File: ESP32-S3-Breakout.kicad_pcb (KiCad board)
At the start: 4 copper layers, 29 x 54.4 mm, 34 parts, among them J1 USB_C_Receptacle_USB2.0, J2 USB_C_Receptacle_USB2.0, J3 Conn_01x21, J4 Conn_01x21, Q1 Q_NPN_BCE, Q2 Q_NPN_BCE, SW1 SW_Push, SW2 SW_Push, U1 USBLC6-2SC6, U2 USBLC6-2SC6, U3 ESP32-S3-WROOM, U4 CH340C, U5 XC6210B332MR, Y1 32.768kHz

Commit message: initial group of modifications.
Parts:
- removed FB2: 500mA?, Inductor_SMD:L_0603_1608Metric
- removed J4: Conn_01x21, Connector_PinHeader_2.54mm:PinHeader_1x21_P2.54mm_Vertical
- removed U4: CH340C, Package_SO:SOIC-16_3.9x9.9mm_P1.27mm
- added C10: 4.7uF, Capacitor_SMD:C_0603_1608Metric, F.Cu at (94.3, 126.6)
- added C11: 1uF, Capacitor_SMD:C_0603_1608Metric, F.Cu at (79.7, 126.5)
- added C12: 10uF, Capacitor_SMD:C_0603_1608Metric, F.Cu at (92.4, 103.3)
- added C13: 10uF, Capacitor_SMD:C_0603_1608Metric, F.Cu at (93.9, 122.2)
- added C14: 10uF, Capacitor_SMD:C_0603_1608Metric, F.Cu at (85.1, 112.1)
- added C15: 100nF, Capacitor_SMD:C_0603_1608Metric, F.Cu at (78.6, 122.1)
- added C16: 100nF, Capacitor_SMD:C_0603_1608Metric, F.Cu at (80.2, 122.1)
- added C17: 100nF, Capacitor_SMD:C_0603_1608Metric, F.Cu at (81.8, 122.1)
- added C18: 15pF, Capacitor_SMD:C_0603_1608Metric, F.Cu at (86.7, 112.1)
- added C19: 15pF, Capacitor_SMD:C_0603_1608Metric, F.Cu at (94.3, 112.1)
- added D3: LED, LED_SMD:LED_0603_1608Metric, F.Cu at (76.8, 130.8)
- added Q3: FDC6330L, Package_TO_SOT_SMD:TSOT-23-6, F.Cu at (91.2, 108.6)
- added R10: 100k, Resistor_SMD:R_0603_1608Metric, F.Cu at (86.7, 108.7)
- added R11: 100, Resistor_SMD:R_0603_1608Metric, F.Cu at (85.1, 108.7)
- added R8: 1k, Resistor_SMD:R_0603_1608Metric, F.Cu at (92.7, 112.1)
- added R9: 100k, Resistor_SMD:R_0603_1608Metric, F.Cu at (88.3, 108.7)
- added U6: USBLC6-2SC6, Package_TO_SOT_SMD:SOT-23-6, F.Cu at (89.7, 121.7)
- added Y2: 12Mhz, Crystal:Crystal_SMD_SeikoEpson_TSX3225-4Pin_3.2x2.5mm, F.Cu at (89.7, 112.1)
- C1: value 22u -> 22uF; footprint Capacitor_SMD:C_0805_2012Metric -> Capacitor_SMD:C_0603_1608Metric
- C2, C4: value 18p -> 15pF
- C3: value 0.1u -> 100nF
- C5: value 1u -> 100nF
- C6, C7: value 0.1u -> 1uF
- C8, C9: value 1u -> 1uF; footprint Capacitor_SMD:C_0805_2012Metric -> Capacitor_SMD:C_0603_1608Metric
- D2: value 1N5819WS -> WS2812B-2020; footprint Diode_SMD:D_SOD-323 -> LED_SMD:LED_WS2812B-2020_PLCC4_2.0x2.0mm
- FB1: value 500mA? -> 500mA; footprint Inductor_SMD:L_0603_1608Metric -> Fuse:Fuse_0603_1608Metric
- J1: value USB_C_Receptacle_USB2.0 -> USB_TYPE_C_16PIN; footprint Connector_USB:USB_C_Receptacle_HRO_TYPE-C-31-M-12 -> Connector_USB:USB_C_Receptacle_GCT_USB4105-xx-A_16P_TopMnt_Horizontal
- J2: value USB_C_Receptacle_USB2.0 -> Conn_01x22; footprint Connector_USB:USB_C_Receptacle_HRO_TYPE-C-31-M-12 -> Connector_PinHeader_2.54mm:PinHeader_1x22_P2.54mm_Vertical; moved to B.Cu
- J3: value Conn_01x21 -> Conn_01x22; footprint Connector_PinHeader_2.54mm:PinHeader_1x21_P2.54mm_Vertical -> Connector_PinHeader_2.54mm:PinHeader_1x22_P2.54mm_Vertical
- Q1, Q2: value Q_NPN_BCE -> S8050
- R3: value 5.1k -> 1k
- R4: value 5.1k -> 10k
- SW1: value SW_Push -> RESET
- SW2: value SW_Push -> BOOT
- U1: value USBLC6-2SC6 -> CH343P; footprint Package_TO_SOT_SMD:SOT-23-6 -> Package_DFN_QFN:QFN-16-1EP_3x3mm_P0.5mm_EP1.7x1.7mm
- U2: value USBLC6-2SC6 -> CH334F; footprint Package_TO_SOT_SMD:SOT-23-6 -> Package_DFN_QFN:QFN-24-1EP_4x4mm_P0.5mm_EP2.7x2.7mm
- U3: value ESP32-S3-WROOM -> ESP32-S3-WROOM-1-N16R8
- moved J2 51.1 mm to (75.6, 74.2), turned to 180 degrees
- moved R5 23.4 mm to (94.3, 125.0), turned to 180 degrees
- moved J3 22.3 mm to (98.4, 74.2)
- moved C8 19.6 mm to (95.5, 122.2), turned to -90 degrees
- moved C3 18.7 mm to (80.0, 100.0), turned to 180 degrees
- moved C1 15.9 mm to (83.2, 100.0), turned to 0 degrees
- moved FB1 15.9 mm to (83.5, 122.1), turned to -90 degrees
- moved SW2 15.8 mm to (79.7, 129.9)
- moved C4 14.6 mm to (93.4, 100.0), turned to 0 degrees
- moved D2 14.5 mm to (81.9, 103.3), turned to 0 degrees
- moved SW1 14.4 mm to (94.3, 129.9)
- moved R1 14.3 mm to (87.1, 122.1), turned to 90 degrees
- moved C7 13.9 mm to (94.3, 117.8), turned to 180 degrees
- moved C2 13.7 mm to (86.4, 100.0), turned to 0 degrees
- moved Y1 13.6 mm to (89.9, 100.2), turned to 0 degrees
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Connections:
- net /CC1_1 renamed /ESP32-S3/CC1_1
- net /CC2_1 renamed /ESP32-S3/CC2_1
- C1 pad 1: +3V3 -> +3.3V
- C2 pad 2: /IO15 -> /GPIO15
- C3 pad 1: +3V3 -> +3.3V
- C4 pad 1: /IO16 -> /GPIO16
- C5 pad 1: /EN -> +3.3V
- C6 pad 1: +3V3 -> /ESP32-S3/3.3VUSB
- C7 pad 1: +3V3 -> GND
- C7 pad 2: GND -> /ESP32-S3/3.3VUSB
- C9 pad 1: +3V3 -> +3.3V
- D1 pad 2: /VBUS1 -> /ESP32-S3/VBUS
- D2 pad 1: Net-(D2-Pad1) -> /LED_OUT
- D2 pad 2: /VBUS2 -> GND
- J1 pad A4: /VBUS1 -> /ESP32-S3/VBUS
- J1 pad A6: /USB_UART_D+ -> /ESP32-S3/USB_D+
- J1 pad A7: /USB_UART_D- -> /ESP32-S3/USB_D-
- J1 pad A9: /VBUS1 -> /ESP32-S3/VBUS
- J1 pad B4: /VBUS1 -> /ESP32-S3/VBUS
- J1 pad B6: /USB_UART_D+ -> /ESP32-S3/USB_D+
- J1 pad B7: /USB_UART_D- -> /ESP32-S3/USB_D-
- J1 pad B9: /VBUS1 -> /ESP32-S3/VBUS
- J3 pad 10: /IO17 -> /GPIO38
- J3 pad 11: /IO18 -> /GPIO37
- J3 pad 12: /IO8 -> /GPIO36
- J3 pad 13: /IO19 -> /GPIO35
- J3 pad 14: /IO20 -> /GPIO0
- J3 pad 15: /IO3 -> /GPIO45
- J3 pad 16: /IO46 -> /GPIO48
- J3 pad 17: /IO9 -> /GPIO47
- J3 pad 18: /IO10 -> /GPIO21
- J3 pad 19: /IO11 -> /ESP_USB+
- J3 pad 2: +3V3 -> /ESP_TX0
- J3 pad 20: /IO12 -> /ESP_USB-
- J3 pad 21: +5V -> GND
- J3 pad 3: /EN -> /ESP_RX0
- J3 pad 4: /IO4 -> /GPIO1
- J3 pad 5: /IO5 -> /GPIO2
- J3 pad 6: /IO6 -> /GPIO42
- J3 pad 7: /IO7 -> /GPIO41
- J3 pad 8: /IO15 -> /GPIO40
- J3 pad 9: /IO16 -> /GPIO39
- Q1 pad 2: /EN -> /ENABLE
- Q1 pad 3: /RTS -> /ESP32-S3/RTS
- Q2 pad 2: /IO0 -> /GPIO0
- Q2 pad 3: /DTR -> /ESP32-S3/DTR
- R3 pad 1: /CC1_2 -> +3.3V
- R3 pad 2: GND -> Net-(D3-A)
- R4 pad 1: /CC2_2 -> /GPIO0
- R4 pad 2: GND -> +3.3V
- R5 pad 1: +3V3 -> +3.3V
- R5 pad 2: /EN -> /ENABLE
- R6 pad 1: /DTR -> /ESP32-S3/DTR
- R7 pad 1: /RTS -> /ESP32-S3/RTS
- SW1 pad 1: /IO0 -> /ENABLE
- SW2 pad 1: /EN -> /GPIO0
- U1 pad 1: /IO19 -> /ESP32-S3/3.3VUSB
- U1 pad 3: /IO20 -> /ESP32-S3/3.3VUSB
- U1 pad 4: /USB_D+ -> /ESP_RX0
- U1 pad 5: /VBUS2 -> /ESP_TX0
- U1 pad 6: /USB_D- -> /ESP32-S3/3.3VUSB
- U2 pad 1: /UART_D- -> unconnected-(U2-~{OVCUR}-Pad1)
- U2 pad 2: GND -> unconnected-(U2-Pad2)
- U2 pad 3: /UART_D+ -> Net-(U2-XOUT)
- U2 pad 4: /USB_UART_D+ -> Net-(U2-XIN)
- U2 pad 5: /VBUS1 -> unconnected-(U2-D-4-Pad5)
- U2 pad 6: /USB_UART_D- -> unconnected-(U2-D+4-Pad6)
- U3 pad 10: /IO17 -> /GPIO17
- U3 pad 11: /IO18 -> /GPIO18
- U3 pad 12: /IO8 -> /GPIO8
- U3 pad 13: /IO19 -> /ESP_USB-
- U3 pad 14: /IO20 -> /ESP_USB+
- U3 pad 15: /IO3 -> /GPIO3
- U3 pad 16: /IO46 -> /GPIO46
- U3 pad 17: /IO9 -> /GPIO9
- U3 pad 18: /IO10 -> /GPIO10
- U3 pad 19: /IO11 -> /GPIO11
- U3 pad 2: +3V3 -> +3.3V
- U3 pad 20: /IO12 -> /GPIO12
- U3 pad 21: /IO13 -> /GPIO13
- U3 pad 22: /IO14 -> /GPIO14
- U3 pad 23: /IO21 -> /GPIO21
- U3 pad 24: /IO47 -> /GPIO47
- U3 pad 25: /IO48 -> /GPIO48
- U3 pad 26: /IO45 -> /GPIO45
- U3 pad 27: /IO0 -> /GPIO0
- U3 pad 28: /IO35 -> /GPIO35
- U3 pad 29: /IO36 -> /GPIO36
- U3 pad 3: /EN -> /ENABLE
- U3 pad 30: /IO37 -> /GPIO37
- U3 pad 31: /IO38 -> /GPIO38
- U3 pad 32: /IO39 -> /GPIO39
- U3 pad 33: /IO40 -> /GPIO40
- U3 pad 34: /IO41 -> /GPIO41
- U3 pad 35: /IO42 -> /GPIO42
- U3 pad 36: /RXD0 -> /ESP_RX0
- U3 pad 37: /TXD0 -> /ESP_TX0
- U3 pad 38: /IO2 -> /GPIO2
- U3 pad 39: /IO1 -> /GPIO1
- U3 pad 4: /IO4 -> /GPIO4
- U3 pad 5: /IO5 -> /GPIO5
- U3 pad 6: /IO6 -> /GPIO6
- U3 pad 7: /IO7 -> /GPIO7
- U3 pad 8: /IO15 -> /GPIO15
- U3 pad 9: /IO16 -> /GPIO16
- U5 pad 5: +3V3 -> +3.3V
- Y1 pad 1: /IO16 -> /GPIO16
- Y1 pad 2: /IO15 -> /GPIO15
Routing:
- net /EN: track 52.0 -> 0.00 mm, vias 4 -> 0
- net GND: track 42.0 -> 0.00 mm, vias 13 -> 0
- net /IO12: track 33.2 -> 0.00 mm, vias 1 -> 0
- net /IO0: track 31.6 -> 0.00 mm, vias 3 -> 0
- net /TXD0: track 31.1 -> 0.00 mm, vias 2 -> 0
- net /RXD0: track 30.5 -> 0.00 mm, vias 2 -> 0
- net /IO13: track 29.3 -> 0.00 mm, vias 1 -> 0
- net /IO19: track 27.6 -> 0.00 mm, vias 1 -> 0
- net /IO11: track 27.4 -> 0.00 mm, vias 1 -> 0
- net /IO14: track 26.7 -> 0.00 mm, vias 1 -> 0
- net /IO10: track 24.5 -> 0.00 mm, vias 1 -> 0
- net /IO21: track 23.8 -> 0.00 mm, vias 1 -> 0
- net /IO20: track 22.6 -> 0.00 mm, vias 1 -> 0
- net /IO9: track 22.2 -> 0.00 mm, vias 1 -> 0
- net /IO47: track 19.7 -> 0.00 mm, vias 1 -> 0
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- added copper zone on B.Cu, net GND
- added copper zone on F.Cu, net GND
- added copper zone on In2.Cu, net GND
- removed copper zone on F.Cu, net +3V3
- removed copper zone on In2.Cu, net +3V3
- removed copper zone on B.Cu, net +5V
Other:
- board size 29 x 54.4 mm -> 25.4 x 63.3 mm
- board text removed: "3V3"
- board text removed: "5V"
- board text removed: "EN"
- board text removed: "ESP32-S3 DEV Module"
- board text removed: "GND"
- board text removed: "IO0"
- board text removed: "IO1"
- board text removed: "IO10"
- board text removed: "IO11"
- board text removed: "IO12"
- board text removed: "IO13"
- board text removed: "IO14"
- board text removed: "IO15"
- board text removed: "IO16"
- board text removed: "IO17"
- board text removed: "IO18"
- board text removed: "IO19"
- board text removed: "IO2"
- board text removed: "IO20"
- board text removed: "IO21"
- board text removed: "IO3"
- board text removed: "IO35"
- board text removed: "IO36"
- board text removed: "IO37"
- board text removed: "IO38"
- board text removed: "IO39"
- board text removed: "IO4"
- board text removed: "IO40"
- board text removed: "IO41"
- board text removed: "IO42"
- board text removed: "IO45"
- board text removed: "IO46"
- board text removed: "IO47"
- board text removed: "IO48"
- board text removed: "IO5"
- board text removed: "IO6"
- board text removed: "IO7"
- board text removed: "IO8"
- board text removed: "IO9"
- board text removed: "RXD0"
- board text removed: "Rev 1 12/2022"
- board text removed: "TXD0"
- board text removed: "UART"
- board text removed: "USB"

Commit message: board is fully routed.
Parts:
- U1: footprint Package_DFN_QFN:QFN-16-1EP_3x3mm_P0.5mm_EP1.7x1.7mm -> Package_DFN_QFN:QFN-16-1EP_3x3mm_P0.5mm_EP1.7x1.7mm_ThermalVias
- U2: footprint Package_DFN_QFN:QFN-24-1EP_4x4mm_P0.5mm_EP2.7x2.7mm -> Package_DFN_QFN:QFN-24-1EP_4x4mm_P0.5mm_EP2.7x2.7mm_ThermalVias
- moved Q1 0.95 mm to (79.1, 108.8)
- moved Q2 0.95 mm to (79.1, 112.4)
- moved R6 0.95 mm to (81.9, 112.4)
- moved R7 0.95 mm to (81.9, 108.8)
- turned D2 to 90 degrees
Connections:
- U2 pad 10: /ESP32-S3/UART_D+ -> /ESP_USB+
- U2 pad 11: /ESP_USB- -> /ESP32-S3/UART_D-
- U2 pad 12: /ESP_USB+ -> /ESP32-S3/UART_D+
- U2 pad 9: /ESP32-S3/UART_D- -> /ESP_USB-
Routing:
- net +3.3V: track 0.00 -> 112.6 mm, vias 0 -> 2
- net /ENABLE: track 0.00 -> 94.8 mm, vias 0 -> 2
- net /GPIO0: track 0.00 -> 68.5 mm, vias 0 -> 3
- net /ESP_TX0: track 0.00 -> 60.5 mm, vias 0 -> 2
- net /ESP_RX0: track 0.00 -> 54.3 mm, vias 0 -> 3
- net +5V: track 0.00 -> 53.3 mm, vias 0 -> 3
- net /ESP_USB-: track 0.00 -> 51.1 mm, vias 0 -> 3
- net /ESP32-S3/3.3VUSB: track 0.00 -> 47.4 mm, vias 0 -> 2
- net /ESP_USB+: track 0.00 -> 47.4 mm, vias 0 -> 3
- net /GPIO38: track 0.00 -> 36.4 mm, vias 0 -> 2
- net /ESP32-S3/VBUS: track 0.00 -> 35.6 mm, vias 0 -> 5
- net /GPIO15: track 0.00 -> 34.8 mm, vias 0 -> 2
- net /GPIO16: track 0.00 -> 33.6 mm, vias 0 -> 3
- net /GPIO14: track 0.00 -> 33.2 mm, vias 0 -> 1
- net /GPIO13: track 0.00 -> 30.4 mm, vias 0 -> 1
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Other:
- board size 25.4 x 63.3 mm -> 25.4 x 60 mm

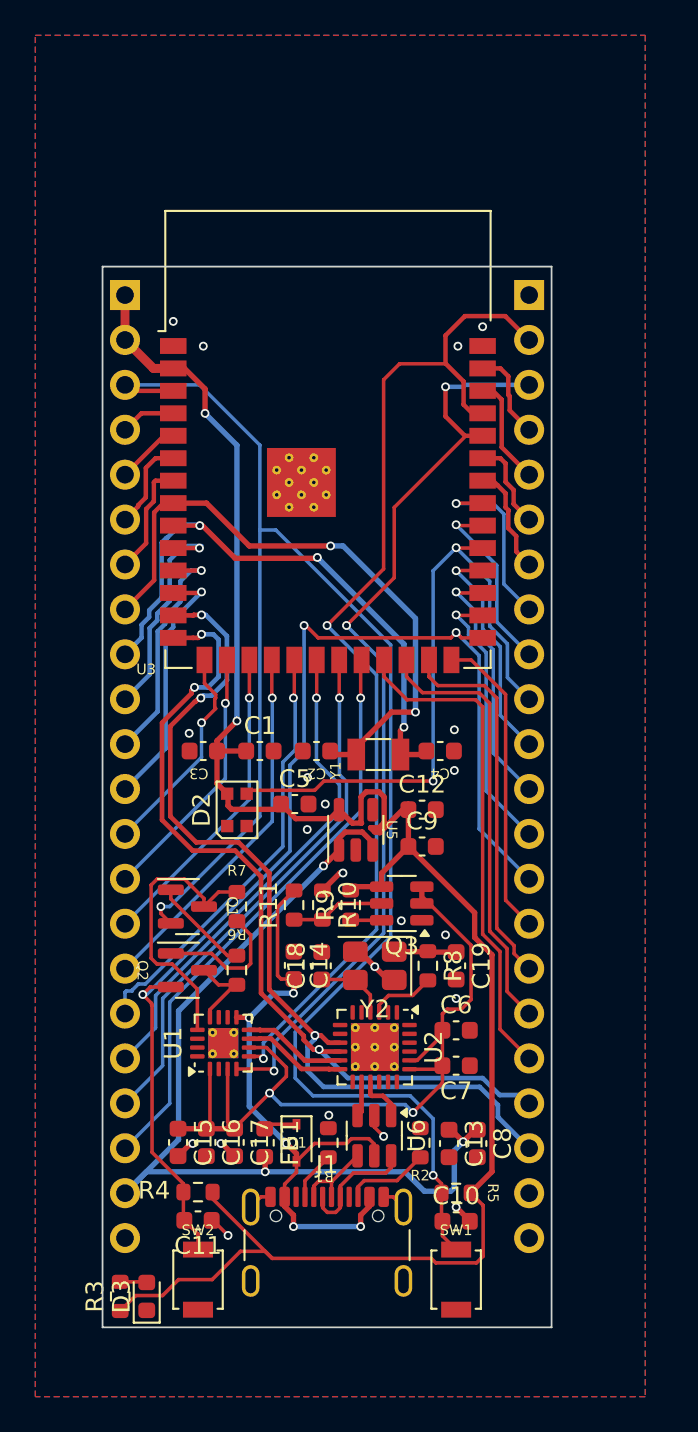
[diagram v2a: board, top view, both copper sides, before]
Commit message: fully routed, erc+drc pass, 3d models
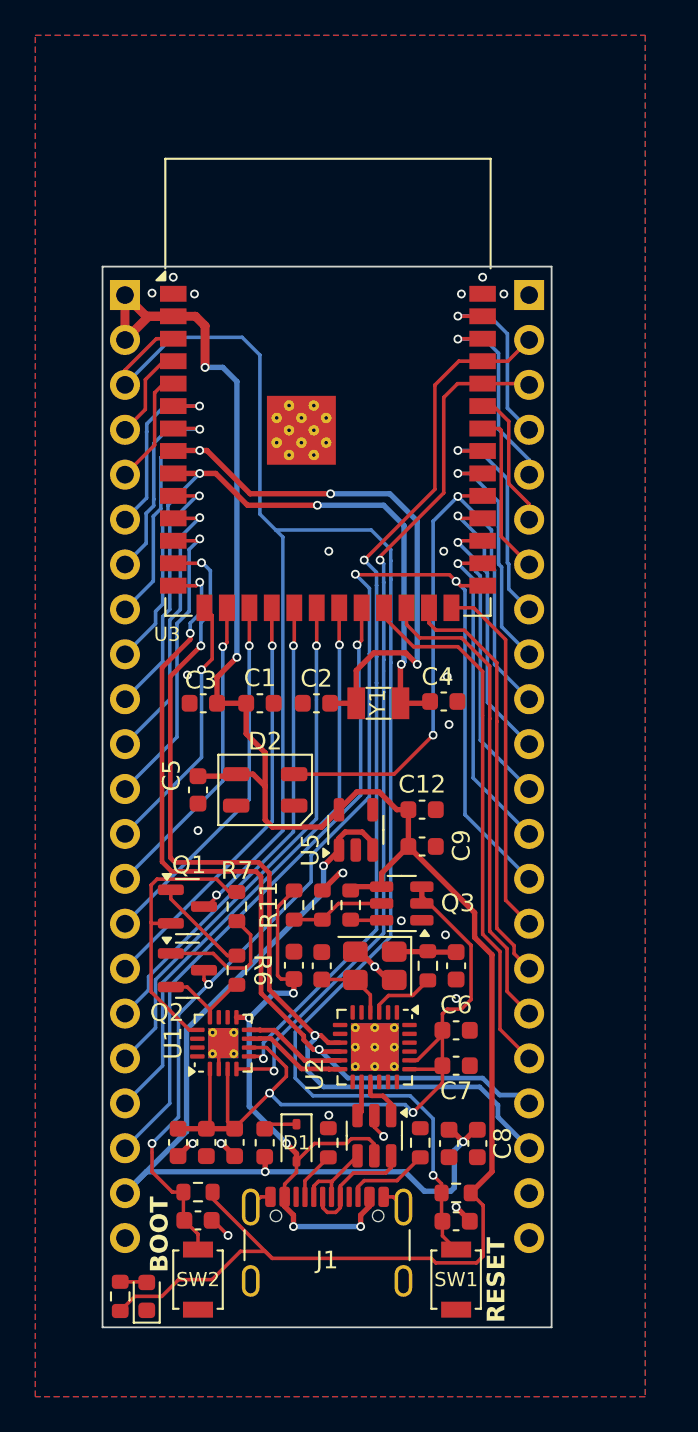
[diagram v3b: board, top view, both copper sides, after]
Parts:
- D2: value WS2812B-2020 -> WS2812B-Mini; footprint LED_SMD:LED_WS2812B-2020_PLCC4_2.0x2.0mm -> LED_SMD:LED_WS2812B-Mini_PLCC4_3.5x3.5mm
- moved C5 5.53 mm to (79.7, 102.2), turned to -90 degrees
- moved U3 2.95 mm to (87.0, 79.4)
- moved Y1 2.90 mm to (89.9, 97.3)
- moved C4 2.81 mm to (93.6, 97.2)
- moved C1 2.70 mm to (83.2, 97.3)
- moved C2 2.70 mm to (86.4, 97.3)
- moved C3 2.70 mm to (80.0, 97.3)
- moved D2 1.96 mm to (83.5, 102.2), turned to 0 degrees
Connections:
- D2 pad 1: /LED_OUT -> +3.3V
- D2 pad 2: GND -> /LED_OUT
- D2 pad 3: /GPIO38 -> GND
- D2 pad 4: +3.3V -> /GPIO38
- Q1 pad 2: /ENABLE -> /ESP32-S3/RTS
- Q1 pad 3: /ESP32-S3/RTS -> /ENABLE
- Q2 pad 2: /GPIO0 -> /ESP32-S3/DTR
- Q2 pad 3: /ESP32-S3/DTR -> /GPIO0
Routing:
- net /ESP_TX0: track 60.5 -> 50.0 mm
- net /GPIO15: track 34.8 -> 42.8 mm, vias 2 -> 3
- net /ENABLE: track 94.8 -> 102.8 mm
- net /GPIO2: track 5.59 -> 11.6 mm, vias 0 -> 1
- net /GPIO6: track 5.19 -> 10.8 mm, vias 0 -> 1
- net /GPIO7: track 6.46 -> 12.0 mm, vias 0 -> 1
- net /GPIO1: track 5.15 -> 10.6 mm, vias 0 -> 1
- net /ESP_RX0: track 54.3 -> 49.5 mm, vias 3 -> 2
- net /GPIO16: track 33.6 -> 38.0 mm
- net /GPIO41: track 5.61 -> 9.34 mm
- net /GPIO0: track 68.5 -> 71.9 mm, vias 3 -> 4
- net +3.3V: track 112.6 -> 116.0 mm
- net /GPIO39: track 10.6 -> 13.7 mm
- net /GPIO14: track 33.2 -> 36.3 mm
- net /ESP_USB-: track 51.1 -> 54.2 mm
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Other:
- board text added: "BOOT"
- board text added: "RESET"

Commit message: silkscreen
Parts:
- added S1: Logo_Open_Hardware_Small, Symbol:OSHW-Logo_5.7x6mm_SilkScreen, F.Cu at (87.0, 75.9)
- moved C5 1.72 mm to (79.7, 103.9)
- moved D2 1.72 mm to (83.5, 103.9)
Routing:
- net +3.3V: track 116.0 -> 118.7 mm
- net /GPIO38: track 37.4 -> 39.5 mm
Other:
- board text added: "Design by Zach Hoeken https://github.com/hoeken/ESP32-S3-Template"
